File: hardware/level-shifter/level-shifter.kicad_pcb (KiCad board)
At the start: 2 copper layers, 59.7 x 63.4 mm, 49 parts, among them IC1 NXB0104PW-Q100J, IC10 NXB0104PW-Q100J, IC2 NXB0104PW-Q100J, IC3 NXB0104PW-Q100J, IC4 NXB0104PW-Q100J, IC5 NXB0104PW-Q100J, IC6 NXB0104PW-Q100J, IC7 NXB0104PW-Q100J, IC8 NXB0104PW-Q100J, IC9 NXB0104PW-Q100J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

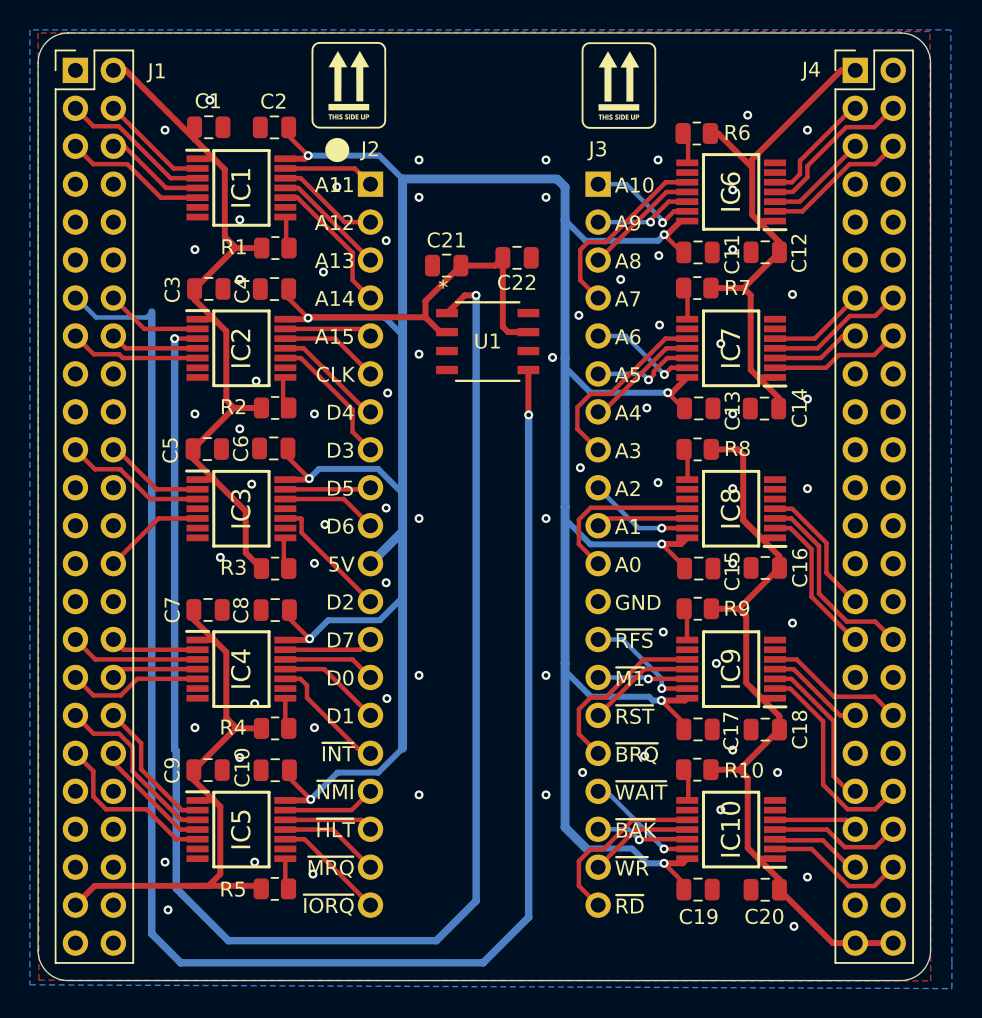
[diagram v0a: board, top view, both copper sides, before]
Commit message: changed PCB to include FlipFlop
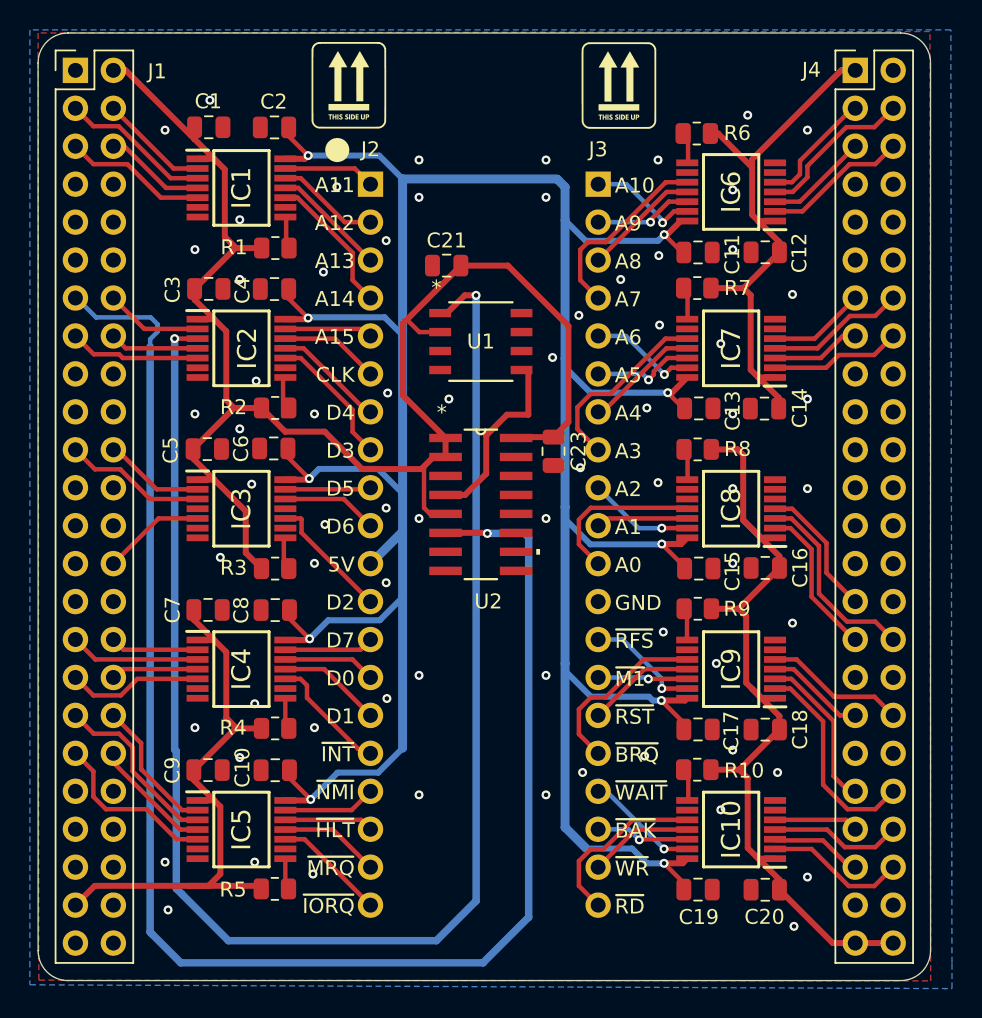
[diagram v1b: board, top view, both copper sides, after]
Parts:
- removed C22: 100nF, Capacitor_SMD:C_0805_2012Metric
- added C23: 100nF, Capacitor_SMD:C_0805_2012Metric, F.Cu at (152.7, 86.5)
- added U2: CD74AC109M96, CD74AC109M96:CD74AC109M96, F.Cu at (147.8, 90.0)
- moved U1 0.46 mm to (147.8, 79.2)
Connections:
- C21 pad 2: +5V -> +3V3UL
- J1 pad 13: PLLCLK -> DOUBLE_CLK
- U1 pad 2: +5V -> +3V3UL
- U1 pad 4: unconnected-(U1-S1-Pad4) -> GND
- U1 pad 6: unconnected-(U1-S0-Pad6) -> GND
- U1 pad 7: +5V -> unconnected-(U1-OE-Pad7)
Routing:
- net DOUBLE_CLK: track 0.00 -> 105.7 mm, vias 0 -> 1
- net PLLCLK: track 111.3 -> 12.3 mm, vias 1 -> 0
- net +3V3UL: track 50.2 -> 109.3 mm
- net +5V: track 231.4 -> 207.3 mm
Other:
- board text added: "Z80 <-> Narvi S7 Translation Board Moid Meghani Pranav Tenneti Neeraj Anantha Daniel McIver Hirsch Prasad"
- board text removed: "Z80 <-> Narvi S7 Translation Board April Douglas Connor Leu"

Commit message: redoing clock for tester
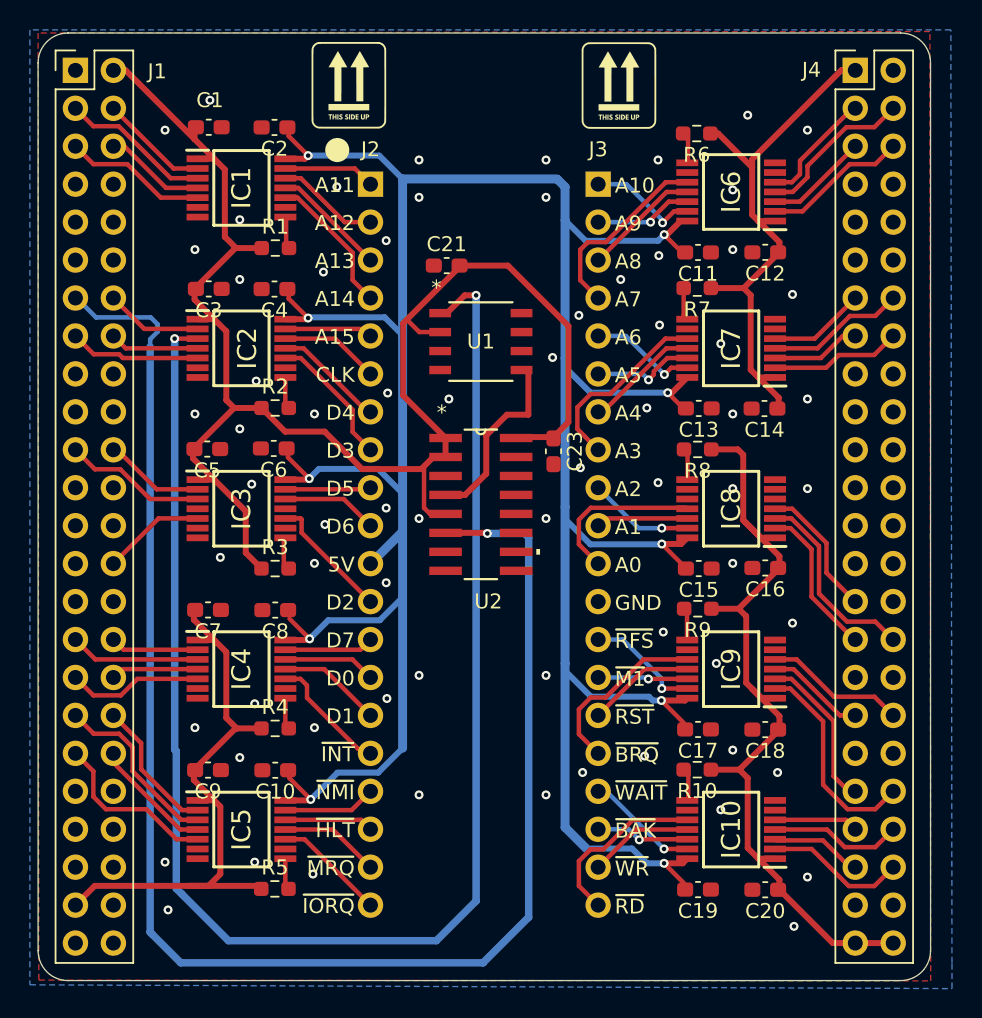
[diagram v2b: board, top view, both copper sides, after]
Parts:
- C1, C10, C11, C12, C13, C14, C15, C16, C17, C18, C19, C2, C20, C21, C23, C3, C4, C5, C6, C7, C8, C9: footprint Capacitor_SMD:C_0805_2012Metric -> Capacitor_SMD:C_0603_1608Metric_Pad1.08x0.95mm_HandSolder
- R1, R10, R2, R3, R4, R5, R6, R7, R8, R9: footprint Resistor_SMD:R_0805_2012Metric -> Resistor_SMD:R_0603_1608Metric_Pad0.98x0.95mm_HandSolder
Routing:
- net +5V: track 207.3 -> 207.9 mm
- net Net-(IC2-OE): track 2.66 -> 2.14 mm
